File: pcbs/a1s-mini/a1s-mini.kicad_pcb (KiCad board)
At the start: 2 copper layers, 69 x 56 mm, 87 parts, among them J1 UART1, J2 SJ-3524-SMT-TR-PI, J3 Audio Out, J4 UART0, J5 USB4105-GF-A, J6 USB4105-GF-A, Q1 BC818, Q2 BC818, Q3 BC818, Q4 BC818, Q5 BC818, U1 ESP32 A1S, U2 AZ1117CH-3.3TRG1, U3 CP2102N, U4 CP2102N

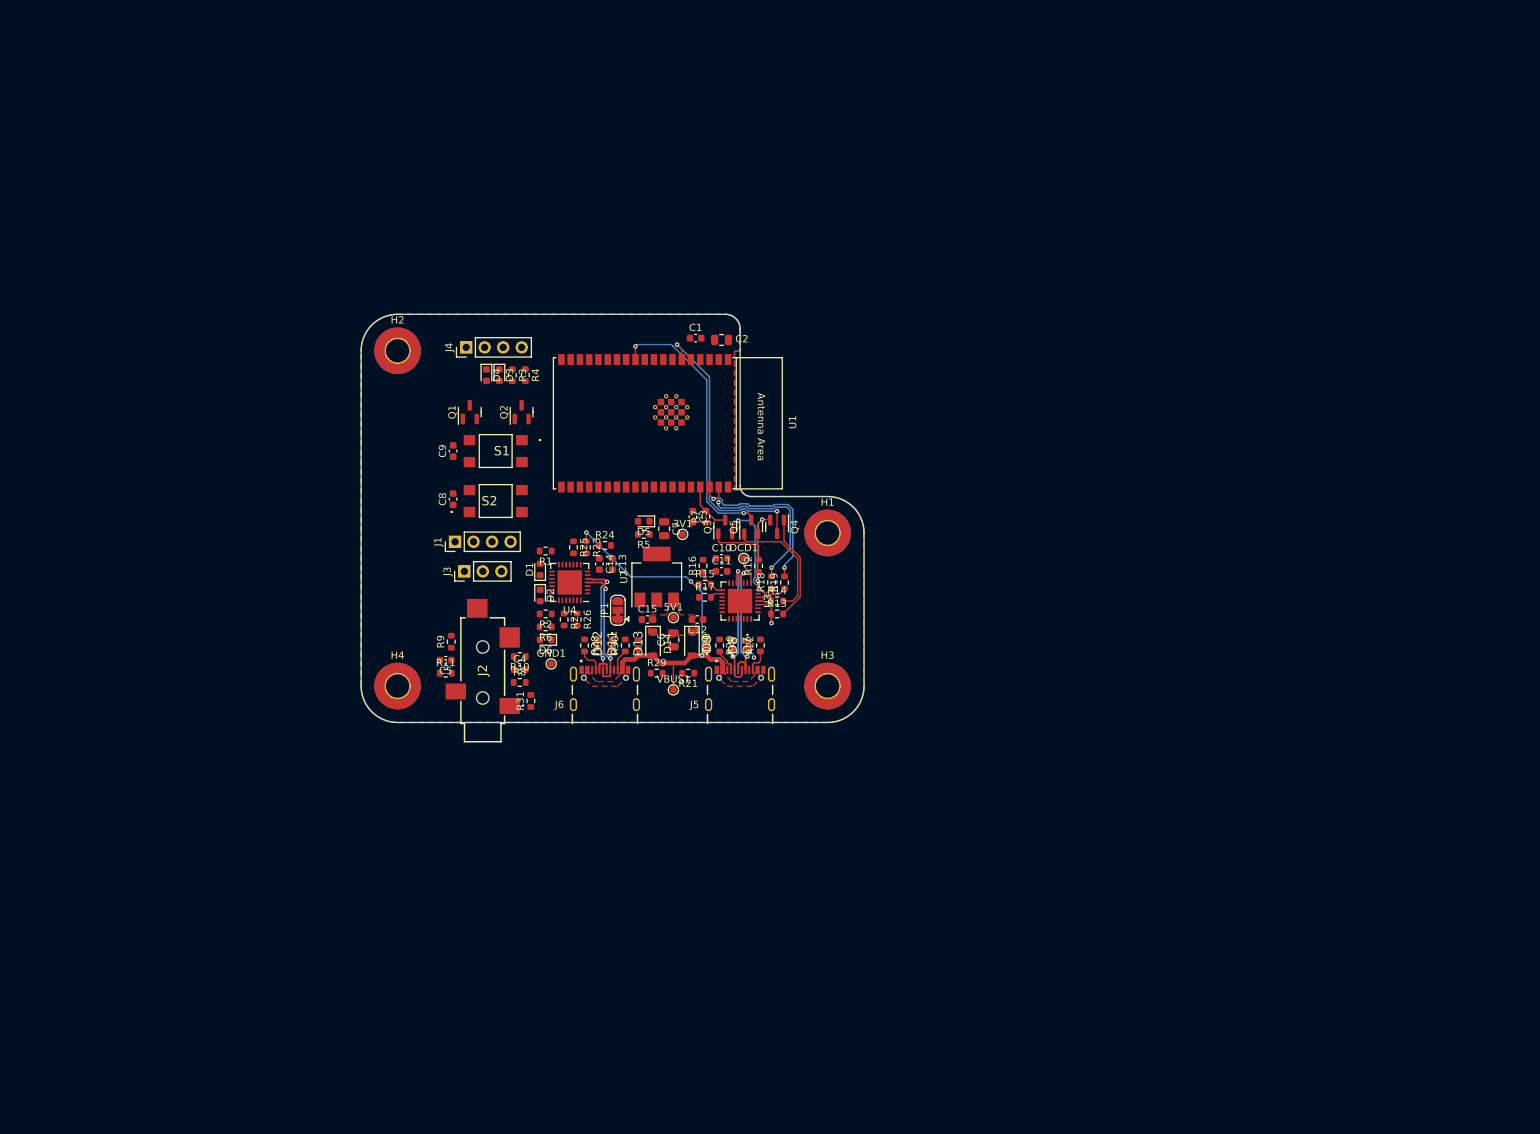
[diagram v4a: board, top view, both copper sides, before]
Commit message: Restart A1S mini
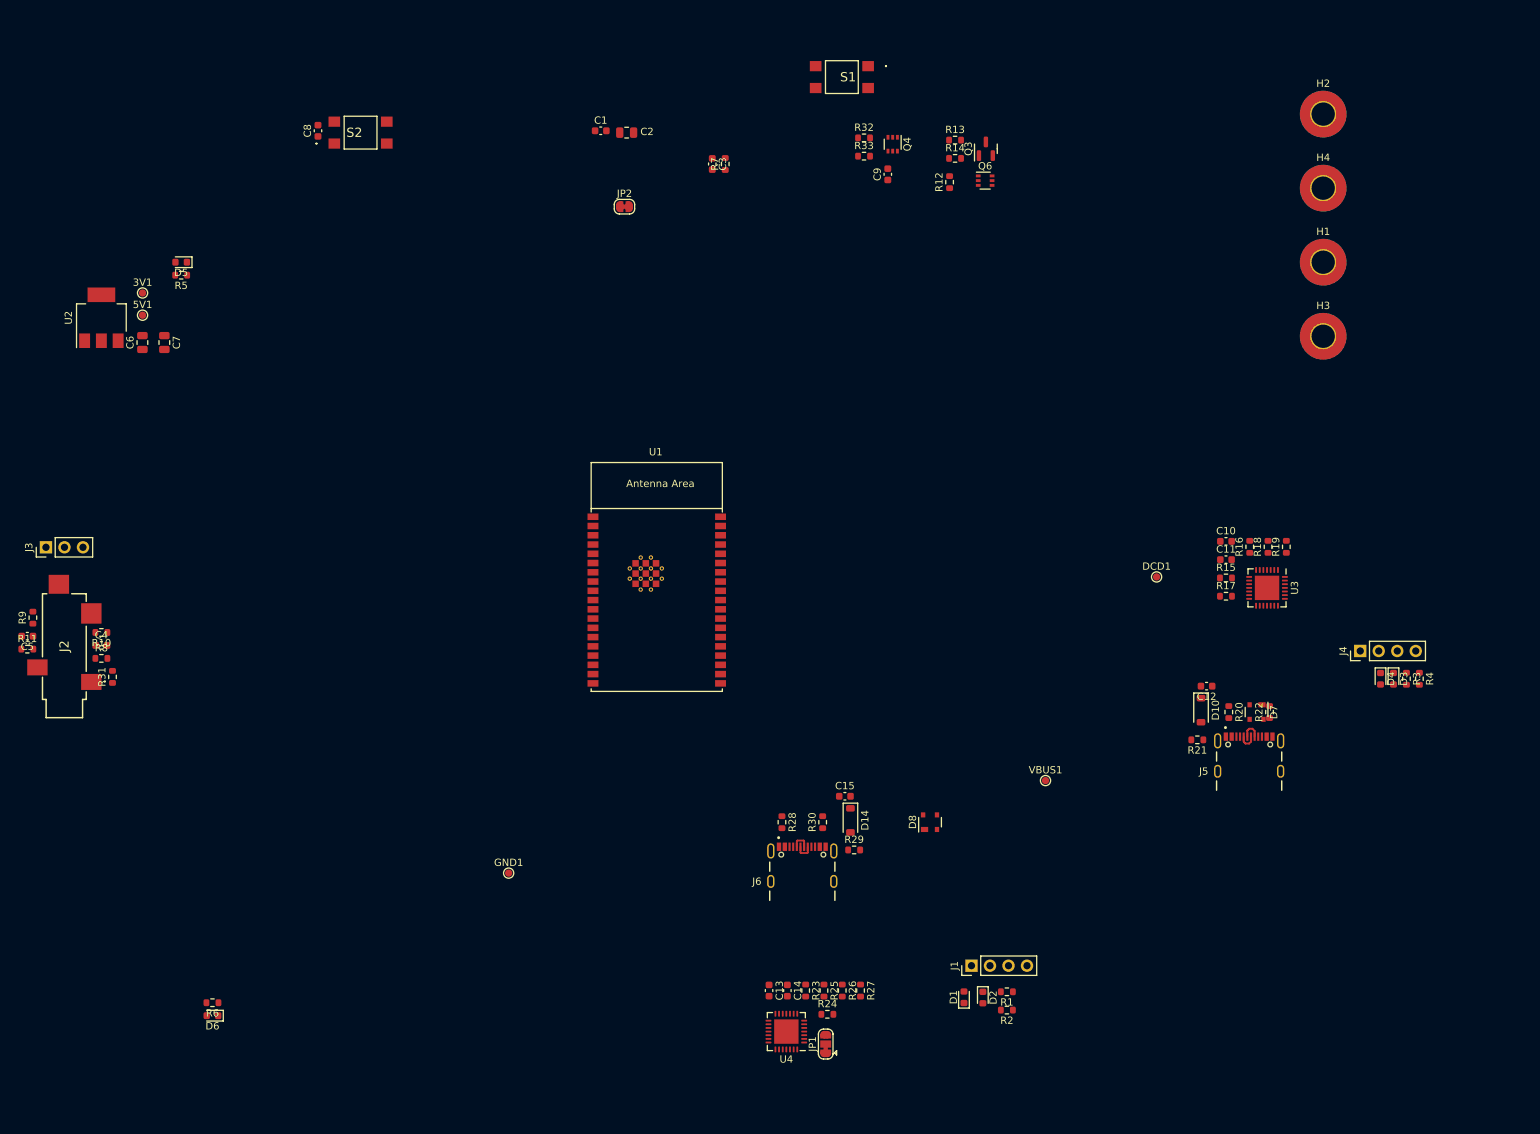
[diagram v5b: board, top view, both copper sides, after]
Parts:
- removed D11, D12, D13, D9: TVS 5.6V, SamacSys_Parts:CPDUC5V0RHF
- removed Q1, Q2, Q5: BC818, Package_TO_SOT_SMD:SOT-23
- added JP2: SolderJumper_2_Bridged, Jumper:SolderJumper-2_P1.3mm_Bridged_RoundedPad1.0x1.5mm, F.Cu at (142.4, 46.0)
- added Q6: BC847BS, Package_TO_SOT_SMD:SOT-363_SC-70-6, F.Cu at (191.9, 42.4)
- added R32: 10K 1%, Resistor_SMD:R_0603_1608Metric, F.Cu at (175.3, 36.5)
- added R33: 10K 1%, Resistor_SMD:R_0603_1608Metric, F.Cu at (175.3, 39.0)
- D7, D8: value TVS 5.6V -> SP0503BAHT; footprint SamacSys_Parts:CPDUC5V0RHF -> Package_TO_SOT_SMD:SOT-143
- Q4: value BC818 -> BC847BS; footprint Package_TO_SOT_SMD:SOT-23 -> Package_TO_SOT_SMD:SOT-363_SC-70-6
- R7: value 0R -> 10K 1%
- moved H4 144.2 mm to (238.3, 43.4)
- moved H2 131.1 mm to (238.3, 33.3)
- moved D3 129.6 mm to (247.9, 110.7)
- moved D4 129.6 mm to (246.1, 110.7)
- moved J4 129.6 mm to (243.3, 106.9)
- moved R3 129.6 mm to (249.7, 110.7)
- moved R4 129.6 mm to (251.4, 110.7)
- moved J1 91.7 mm to (190.0, 150.1)
- moved R1 87.5 mm to (194.9, 153.7)
- moved U2 84.1 mm to (70.6, 61.2)
- moved 5V1 83.8 mm to (76.3, 60.9)
- moved C6 83.5 mm to (76.2, 64.6)
- moved R2 83.4 mm to (194.9, 156.2)
- moved H3 83.2 mm to (238.3, 63.8)
- moved D1 82.6 mm to (189.0, 154.4)
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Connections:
- D7 pad 2: /CP2102_0/D+ -> VBUS
- D8 pad 1: /CP2102_0/D- -> GND
- D8 pad 2: GND -> VBUS
- Q4 pad 1: Net-(Q4-B) -> GND
- Q4 pad 2: DTR0 -> Net-(Q4A-B1)
- R13 pad 2: Net-(Q4-B) -> Net-(Q6A-B1)
- U1 pad 10: unconnected-(U1-IO15-Pad10) -> Net-(JP2-A)
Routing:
- net VBUS: track 53.7 -> 0.00 mm, vias 3 -> 0
- net IO0: track 38.7 -> 0.00 mm, vias 2 -> 0
- net IO2: track 37.8 -> 0.00 mm, vias 2 -> 0
- net RTS0: track 24.3 -> 0.00 mm, vias 2 -> 0
- net TXD0: track 23.7 -> 0.00 mm, vias 2 -> 0
- net RXD0: track 23.2 -> 0.00 mm, vias 2 -> 0
- net /CP2102_0/D-: track 19.5 -> 2.60 mm, vias 2 -> 0
- net /CP2102_0/D+: track 19.6 -> 2.85 mm, vias 2 -> 0
- net Net-(Q6B-B2): track 16.6 -> 0.00 mm
- net /CP2102_1/D-: track 19.0 -> 2.63 mm, vias 2 -> 0
- net /CP2102_1/D+: track 19.0 -> 2.63 mm, vias 2 -> 0
- net Net-(Q4-B): track 14.8 -> 0.00 mm
- net DTR0: track 14.5 -> 0.00 mm, vias 2 -> 0
- net Net-(Q3-B): track 8.76 -> 0.00 mm
- net EN: track 6.77 -> 0.00 mm
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- removed copper zone on F.Cu, net +5V
- removed copper zone on B.Cu, net GND
- removed copper zone on F.Cu, net GND
- removed copper zone on F.Cu, net VBUS
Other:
- board outline removed

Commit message: Additional VBus capacitor
Also making sure that the CP2102N is not bus-powered, but self-powered
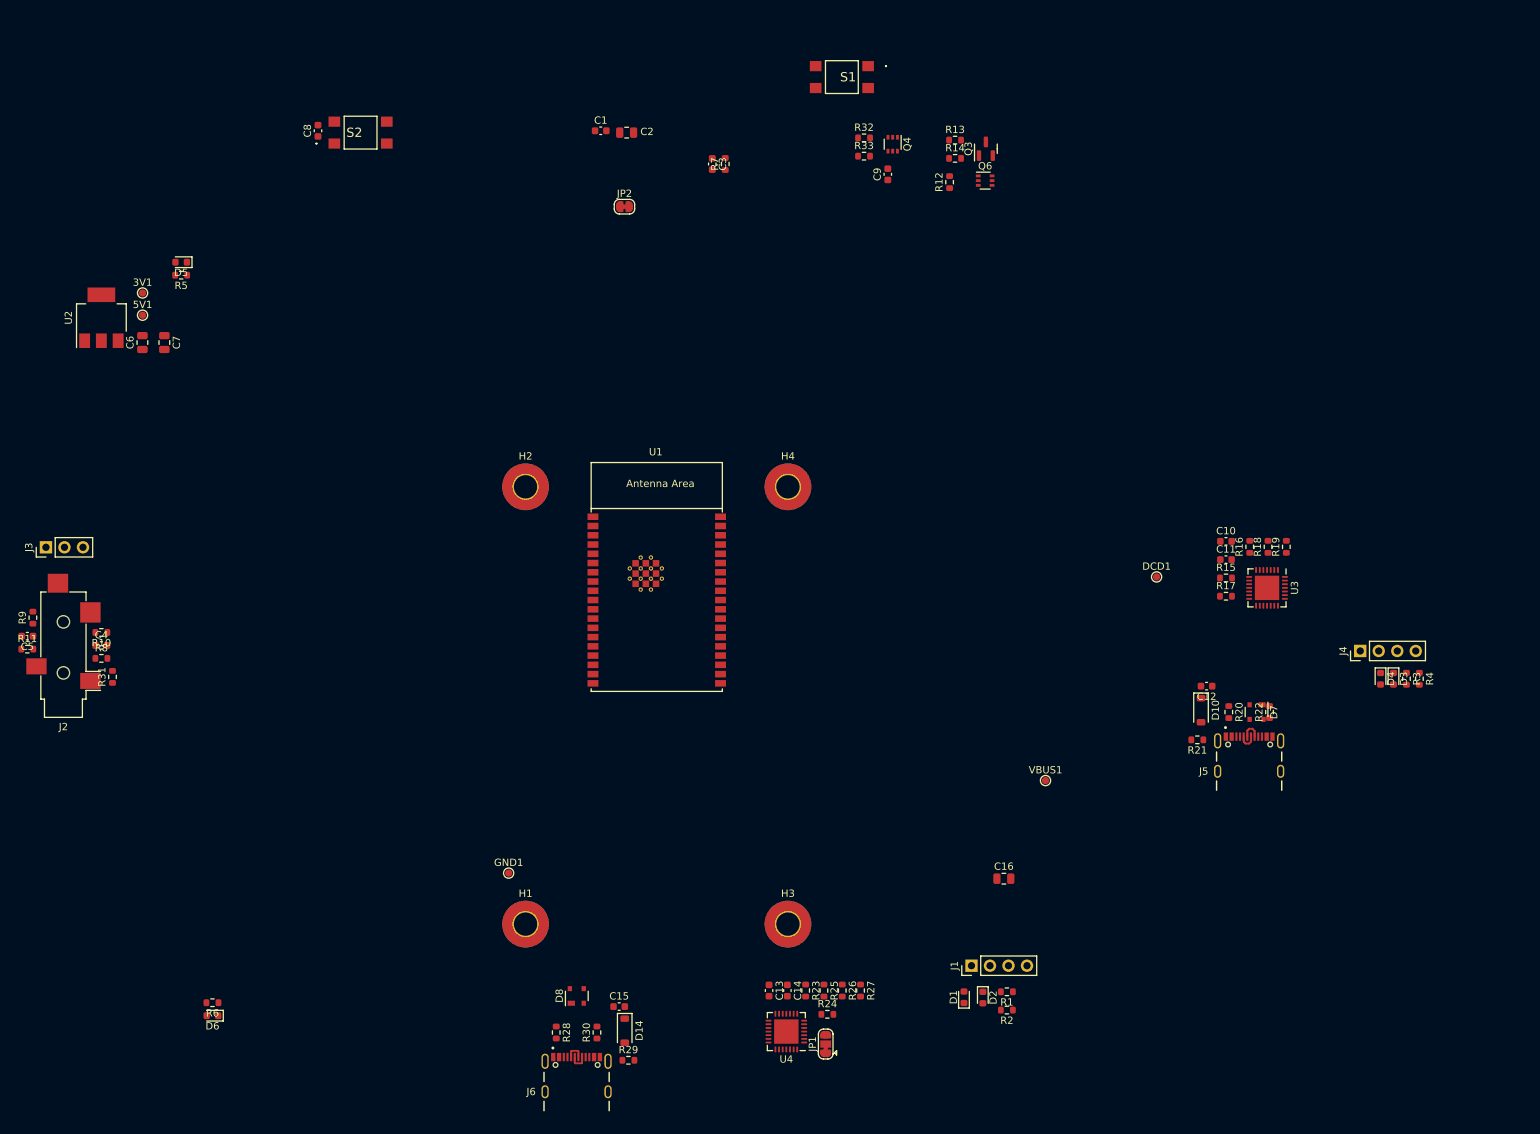
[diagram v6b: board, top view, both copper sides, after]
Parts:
- added C16: 22uF 10V, Capacitor_SMD:C_0805_2012Metric, F.Cu at (194.4, 138.2)
- J2: footprint SamacSys_Parts:SJ3524SMTTRPI -> Connector_Audio:Jack_3.5mm_CUI_SJ-3524-SMT_Horizontal
- moved H1 142.2 mm to (128.8, 144.4)
- moved H2 120.8 mm to (128.8, 84.4)
- moved H3 109.1 mm to (164.8, 144.4)
- moved H4 84.1 mm to (164.8, 84.4)
- moved D8 54.0 mm to (135.8, 154.3)
- moved R28 42.3 mm to (133.0, 159.3)
- moved R29 42.3 mm to (142.9, 163.1)
- moved R30 42.3 mm to (138.6, 159.3)
- moved C15 42.3 mm to (141.7, 155.7)
- moved D14 42.3 mm to (142.4, 159.0)
- moved J6 42.3 mm to (135.8, 167.4)
- moved J2 0.52 mm to (65.4, 107.4), turned to 180 degrees

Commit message: Outline
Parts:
- moved H1 1.00 mm to (128.8, 145.4)
- moved H2 1.00 mm to (128.8, 85.4)
- moved H3 1.00 mm to (164.8, 145.4)
- moved H4 1.00 mm to (164.8, 85.4)
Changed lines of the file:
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@@
     )
   )
-  (footprint "MountingHole:MountingHole_3.2mm_M3_Pad_TopBottom" (layer "F.Cu")
-    (at 128.812 144.409)
+  (footprint "MountingHole:MountingHole_3.2mm_M3_Pad_TopBottom" locked (layer "F.Cu")
+    (at 128.812 145.409)
     (descr "Mounting Hole 3.2mm, M3")
     (tags "mounting hole 3.2mm m3")
@@
     (fp_circle (center 0 0) (end 3.45 0)
       (stroke (width 0.05) (type solid)) (fill none) (layer "F.CrtYd"))
-    (pad "1" thru_hole circle (at 0 0) (size 3.6 3.6) (drill 3.2) (layers "*.Cu" "*.Mask")
+    (pad "1" thru_hole circle locked (at 0 0) (size 3.6 3.6) (drill 3.2) (layers "*.Cu" "*.Mask")
       (net 20 "GND") (pinfunction "1") (pintype "input"))
-    (pad "1" connect circle (at 0 0) (size 6.4 6.4) (layers "F.Cu" "F.Mask")
+    (pad "1" connect circle locked (at 0 0) (size 6.4 6.4) (layers "F.Cu" "F.Mask")
       (net 20 "GND") (pinfunction "1") (pintype "input"))
-    (pad "1" connect circle (at 0 0) (size 6.4 6.4) (layers "B.Cu" "B.Mask")
+    (pad "1" connect circle locked (at 0 0) (size 6.4 6.4) (layers "B.Cu" "B.Mask")
       (net 20 "GND") (pinfunction "1") (pintype "input"))
   )
@@
     )
   )
-  (footprint "MountingHole:MountingHole_3.2mm_M3_Pad_TopBottom" (layer "F.Cu")
-    (at 128.812 84.409)
+  (footprint "MountingHole:MountingHole_3.2mm_M3_Pad_TopBottom" locked (layer "F.Cu")
+    (at 128.812 85.409)
     (descr "Mounting Hole 3.2mm, M3")
     (tags "mounting hole 3.2mm m3")
@@
     (fp_circle (center 0 0) (end 3.45 0)
       (stroke (width 0.05) (type solid)) (fill none) (layer "F.CrtYd"))
-    (pad "1" thru_hole circle (at 0 0) (size 3.6 3.6) (drill 3.2) (layers "*.Cu" "*.Mask")
+    (pad "1" thru_hole circle locked (at 0 0) (size 3.6 3.6) (drill 3.2) (layers "*.Cu" "*.Mask")
       (net 20 "GND") (pinfunction "1") (pintype "input"))
-    (pad "1" connect circle (at 0 0) (size 6.4 6.4) (layers "F.Cu" "F.Mask")
+    (pad "1" connect circle locked (at 0 0) (size 6.4 6.4) (layers "F.Cu" "F.Mask")
       (net 20 "GND") (pinfunction "1") (pintype "input"))
-    (pad "1" connect circle (at 0 0) (size 6.4 6.4) (layers "B.Cu" "B.Mask")
+    (pad "1" connect circle locked (at 0 0) (size 6.4 6.4) (layers "B.Cu" "B.Mask")
       (net 20 "GND") (pinfunction "1") (pintype "input"))
   )
@@
     )
   )
-  (footprint "MountingHole:MountingHole_3.2mm_M3_Pad_TopBottom" (layer "F.Cu")
-    (at 164.812 84.409)
+  (footprint "MountingHole:MountingHole_3.2mm_M3_Pad_TopBottom" locked (layer "F.Cu")
+    (at 164.812 85.409)
     (descr "Mounting Hole 3.2mm, M3")
     (tags "mounting hole 3.2mm m3")
@@
     (fp_circle (center 0 0) (end 3.45 0)
       (stroke (width 0.05) (type solid)) (fill none) (layer "F.CrtYd"))
-    (pad "1" thru_hole circle (at 0 0) (size 3.6 3.6) (drill 3.2) (layers "*.Cu" "*.Mask")
+    (pad "1" thru_hole circle locked (at 0 0) (size 3.6 3.6) (drill 3.2) (layers "*.Cu" "*.Mask")
       (net 20 "GND") (pinfunction "1") (pintype "input"))
-    (pad "1" connect circle (at 0 0) (size 6.4 6.4) (layers "F.Cu" "F.Mask")
+    (pad "1" connect circle locked (at 0 0) (size 6.4 6.4) (layers "F.Cu" "F.Mask")
       (net 20 "GND") (pinfunction "1") (pintype "input"))
-    (pad "1" connect circle (at 0 0) (size 6.4 6.4) (layers "B.Cu" "B.Mask")
+    (pad "1" connect circle locked (at 0 0) (size 6.4 6.4) (layers "B.Cu" "B.Mask")
       (net 20 "GND") (pinfunction "1") (pintype "input"))
   )
@@
     )
   )
-  (footprint "MountingHole:MountingHole_3.2mm_M3_Pad_TopBottom" (layer "F.Cu")
-    (at 164.812 144.409)
+  (footprint "MountingHole:MountingHole_3.2mm_M3_Pad_TopBottom" locked (layer "F.Cu")
+    (at 164.812 145.409)
     (descr "Mounting Hole 3.2mm, M3")
     (tags "mounting hole 3.2mm m3")
@@
     (fp_circle (center 0 0) (end 3.45 0)
       (stroke (width 0.05) (type solid)) (fill none) (layer "F.CrtYd"))
-    (pad "1" thru_hole circle (at 0 0) (size 3.6 3.6) (drill 3.2) (layers "*.Cu" "*.Mask")
+    (pad "1" thru_hole circle locked (at 0 0) (size 3.6 3.6) (drill 3.2) (layers "*.Cu" "*.Mask")
       (net 20 "GND") (pinfunction "1") (pintype "input"))
-    (pad "1" connect circle (at 0 0) (size 6.4 6.4) (layers "F.Cu" "F.Mask")
+    (pad "1" connect circle locked (at 0 0) (size 6.4 6.4) (layers "F.Cu" "F.Mask")
       (net 20 "GND") (pinfunction "1") (pintype "input"))
-    (pad "1" connect circle (at 0 0) (size 6.4 6.4) (layers "B.Cu" "B.Mask")
+    (pad "1" connect circle locked (at 0 0) (size 6.4 6.4) (layers "B.Cu" "B.Mask")
       (net 20 "GND") (pinfunction "1") (pintype "input"))
   )
@@
     )
   )
+  (gr_line (start 123.812 80.409) (end 123.812 150.409)
+    (stroke (width 0.1) (type default)) (layer "Dwgs.User"))
+  (gr_line (start 169.812 80.409) (end 123.812 80.409)
+    (stroke (width 0.1) (type default)) (layer "Dwgs.User"))
+  (gr_line (start 169.812 80.409) (end 169.812 150.409)
+    (stroke (width 0.1) (type default)) (layer "Dwgs.User"))
   (segment (start 227.842 118.689) (end 227.842 117.86) (width 0.254) (layer "F.Cu") (net 19))
   (segment (start 227.842 117.86) (end 227.838 117.856) (width 0.254) (layer "F.Cu") (net 19))

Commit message: PCB layout update
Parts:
- removed D3, D4: 2.1V G 10mA, LED_SMD:LED_0603_1608Metric
- removed R3, R4: 1K 1%, Resistor_SMD:R_0603_1608Metric
- added D11: 2.1V G 10mA, LED_SMD:LED_0603_1608Metric, F.Cu at (166.4, 122.2)
- added D9: 2.1V G 10mA, LED_SMD:LED_0603_1608Metric, F.Cu at (166.4, 125.5)
- added R34: 1K 1%, Resistor_SMD:R_0603_1608Metric, F.Cu at (164.6, 125.5)
- added R35: 1K 1%, Resistor_SMD:R_0603_1608Metric, F.Cu at (164.6, 122.2)
- moved J2 118.5 mm to (183.3, 94.9), turned to -90 degrees
- moved J3 115.1 mm to (177.8, 84.2), turned to -90 degrees
- moved C5 109.4 mm to (169.6, 98.4)
- moved R11 109.4 mm to (169.6, 100.2)
- moved R9 108.5 mm to (169.6, 96.6), turned to 180 degrees
- moved S1 101.7 mm to (126.8, 119.2), turned to -90 degrees
- moved R10 100.1 mm to (169.6, 89.5), turned to 0 degrees
- moved R8 100.1 mm to (169.6, 93.1), turned to 180 degrees
- moved C4 100.1 mm to (169.6, 91.3), turned to 180 degrees
- moved U2 99.6 mm to (149.7, 121.7), turned to 180 degrees
- moved C9 99.2 mm to (126.1, 125.7), turned to 180 degrees
- moved R31 98.7 mm to (169.6, 94.9), turned to 180 degrees
- moved R13 96.2 mm to (129.3, 113.3), turned to 180 degrees
- moved R6 96.2 mm to (165.0, 100.6)
- moved C6 95.8 mm to (155.6, 118.4), turned to -90 degrees
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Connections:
- D1 pad 1: RXD1 -> Net-(D1-K)
- D2 pad 1: TXD1 -> Net-(D2-K)
- J2 pad R: (no net) -> ROUT
- J2 pad S: (no net) -> AGND
- J2 pad T: (no net) -> LOUT
- J2 pad TN: (no net) -> unconnected-(J2-PadTN)
- U3 pad 18: unconnected-(U3-~{RXT}/GPIO.1-Pad18) -> Net-(D2-K)
- U3 pad 19: unconnected-(U3-~{TXT}/GPIO.0-Pad19) -> Net-(D1-K)
- U4 pad 18: unconnected-(U4-~{RXT}/GPIO.1-Pad18) -> Net-(D11-K)
- U4 pad 19: unconnected-(U4-~{TXT}/GPIO.0-Pad19) -> Net-(D9-K)
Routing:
- net /CP2102_0/D+: track 2.85 -> 0.00 mm
- net /CP2102_1/D+: track 2.63 -> 0.00 mm
- net /CP2102_1/D-: track 2.63 -> 0.00 mm
- net /CP2102_0/D-: track 2.60 -> 0.00 mm
